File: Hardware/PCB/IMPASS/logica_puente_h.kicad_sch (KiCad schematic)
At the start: 36 parts, among them Q49 2N7002, Q50 2N7002, Q51 2N7002, Q52 2N7002, Q53 2N7002, Q54 2N7002, Q55 2N7002, Q56 2N7002, Q57 2N7002, Q58 2N7002, Q59 2N7002, Q60 2N7002, Q61 2N7002, Q62 2N7002, Q63 2N7002, Q64 2N7002, Q65 2N7002, Q66 2N7002

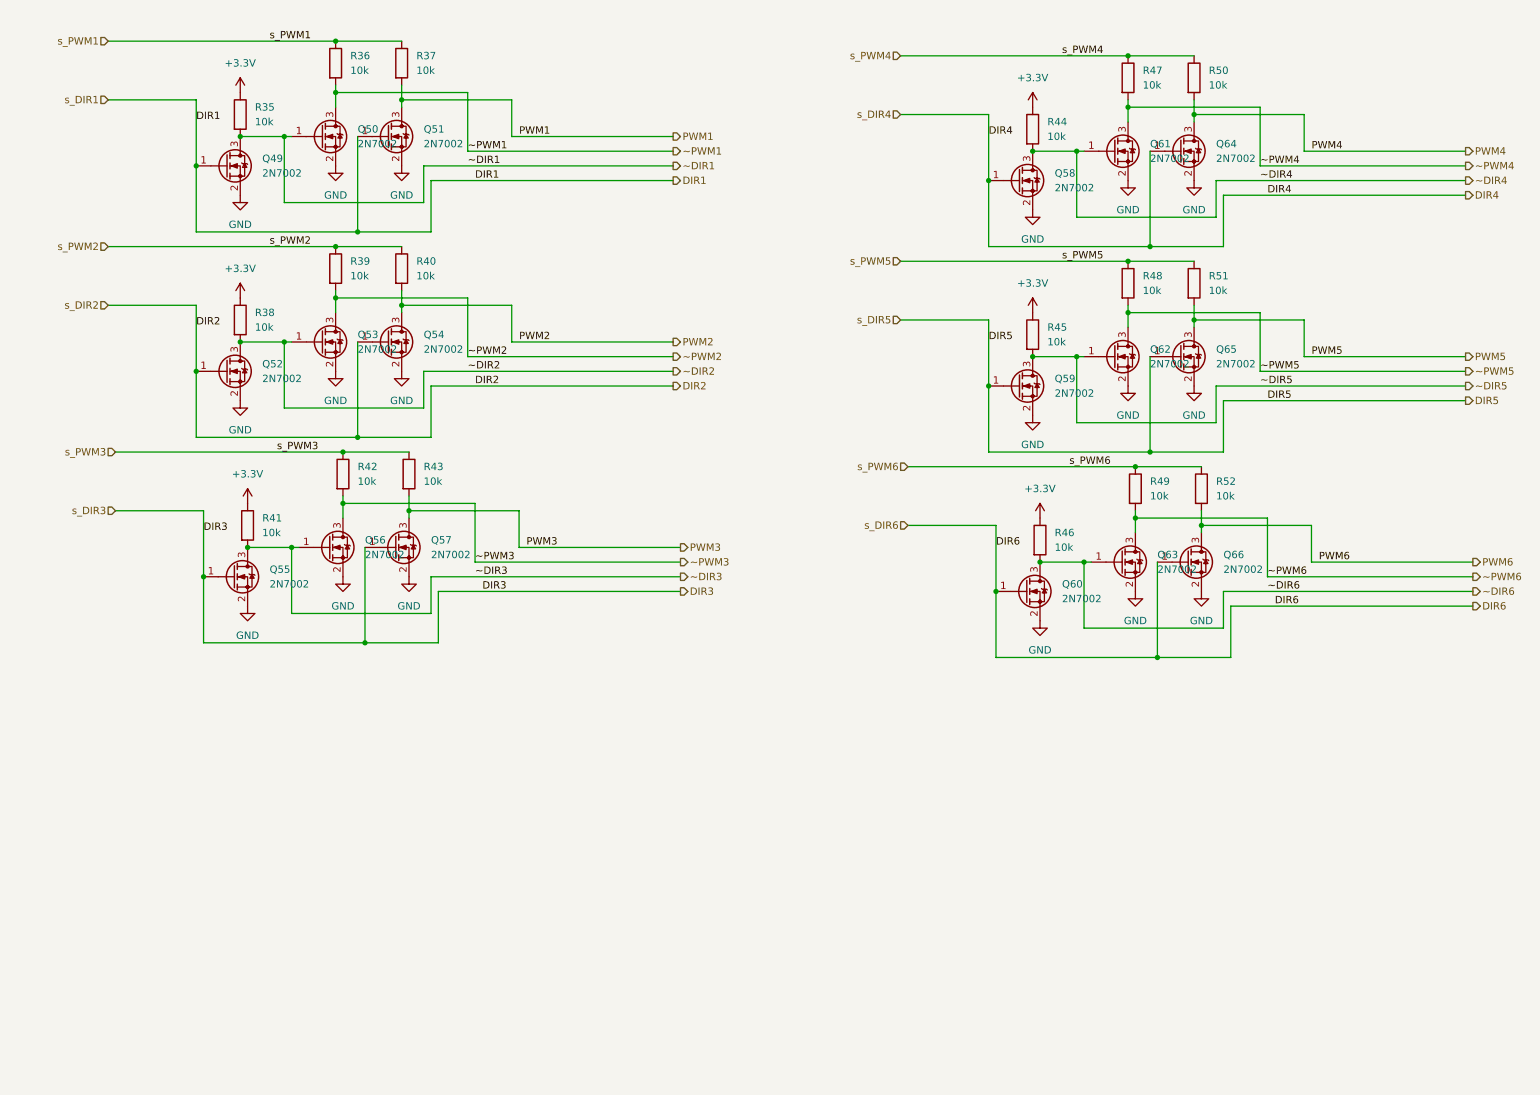
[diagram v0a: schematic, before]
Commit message: Hardware: Update all the logic pcb 	- added ads1015 	- added the logic foe P-MOSFET 	- added I2C connector
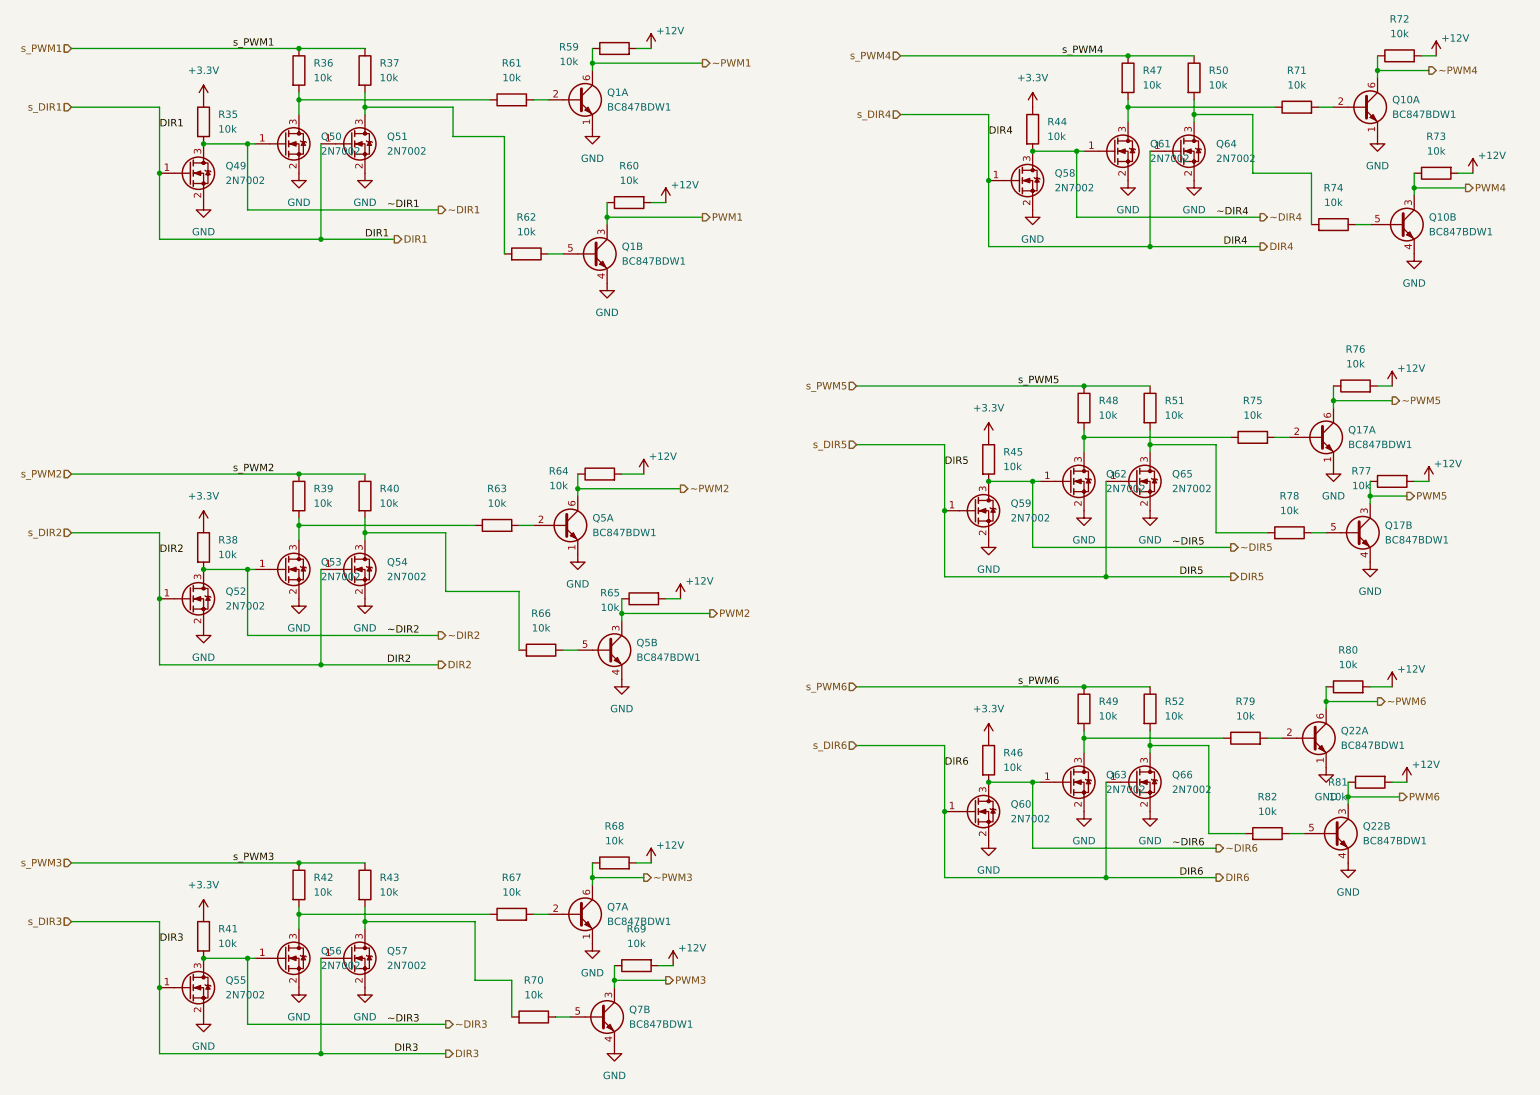
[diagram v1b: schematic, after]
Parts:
- added Q1, Q10, Q17, Q22, Q5, Q7: BC847BDW1, Package_TO_SOT_SMD:SOT-363_SC-70-6, symbol Transistor_BJT:BC847BDW1
- added R59, R60, R61, R62, R63, R64, R65, R66, R67, R68, R69, R70, R71, R72, R73, R74, R75, R76, R77, R78, R79, R80, R81, R82: 10k, Resistor_SMD:R_0603_1608Metric, symbol Device:R
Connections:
- net GND: now also Q1.1 (E1), Q1.4 (E2), Q10.1 (E1), Q10.4 (E2), Q17.1 (E1), Q17.4 (E2), Q22.1 (E1), Q22.4 (E2), Q5.1 (E1), Q5.4 (E2), Q7.1 (E1), Q7.4 (E2)
- net PWM1: now also Q1.3 (C2), R60.1; no longer Q51.3 (D), R37.2
- net PWM2: now also Q5.3 (C2), R65.1; no longer Q54.3 (D), R40.2
- net PWM3: now also Q7.3 (C2), R69.1; no longer Q57.3 (D), R43.2
- net PWM4: now also Q10.3 (C2), R73.1; no longer Q64.3 (D), R50.2
- net PWM5: now also Q17.3 (C2), R77.1; no longer Q65.3 (D), R51.2
- net PWM6: now also Q22.3 (C2), R81.1; no longer Q66.3 (D), R52.2
- net ~PWM1: now also Q1.6 (C1), R59.1; no longer Q50.3 (D), R36.2
- net ~PWM2: now also Q5.6 (C1), R64.1; no longer Q53.3 (D), R39.2
- net ~PWM3: now also Q7.6 (C1), R68.1; no longer Q56.3 (D), R42.2
- net ~PWM4: now also Q10.6 (C1), R72.1; no longer Q61.3 (D), R47.2
- net ~PWM5: now also Q17.6 (C1), R76.1; no longer Q62.3 (D), R48.2
- net ~PWM6: now also Q22.6 (C1), R80.1; no longer Q63.3 (D), R49.2
- new net: Q22.2 (B1), R79.2
- new net: Q5.5 (B2), R66.1
- new net: Q54.3 (D), R40.2, R66.2
- new net: Q64.3 (D), R50.2, R74.2
- new net: Q10.2 (B1), R71.2
- new net: Q50.3 (D), R36.2, R61.1
- new net: Q61.3 (D), R47.2, R71.1
- new net: Q62.3 (D), R48.2, R75.1
- new net: Q17.2 (B1), R75.2
- new net: Q53.3 (D), R39.2, R63.1
- new net: Q10.5 (B2), R74.1
- new net: Q1.5 (B2), R62.1
- new net: Q51.3 (D), R37.2, R62.2
- new net: Q17.5 (B2), R78.1
- new net: Q65.3 (D), R51.2, R78.2
- new net: Q7.2 (B1), R67.2
- new net: Q57.3 (D), R43.2, R70.2
- new net: Q7.5 (B2), R70.1
- new net: Q63.3 (D), R49.2, R79.1
- new net: Q66.3 (D), R52.2, R82.2
- new net: Q1.2 (B1), R61.2
- new net: Q5.2 (B1), R63.2
- new net: Q56.3 (D), R42.2, R67.1
- new net: Q22.5 (B2), R82.1
- new net +12V: R59.2, R60.2, R64.2, R65.2, R68.2, R69.2, R72.2, R73.2, R76.2, R77.2, R80.2, R81.2
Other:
- moved on the sheet: Q49, Q50, Q51, Q52, Q53, Q54, Q55, Q56, Q57, Q59, Q60, Q62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
